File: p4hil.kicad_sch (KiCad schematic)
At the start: 9 parts, among them J10 Conn_01x22, J11 Conn_01x22, J12 Conn_01x22, J2 Conn_01x08, J4 Conn_01x10, J5 Conn_01x22, J6 Conn_01x22, J7 Conn_01x22, J9 Conn_01x06

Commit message: More brainstorming
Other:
- sheet P4 ports: added CHIP_PU, GPIO0/ADC, GPIO10/ADC, GPIO11/ADC, GPIO12/ADC, GPIO13/ADC, GPIO14/ADC, GPIO15/ADC, GPIO16/ADC, GPIO17/ADC, GPIO18/ADC, GPIO19/ADC, GPIO1/ADC, GPIO20/ADC, GPIO21/ADC, GPIO22/ADC, GPIO23/ADC, GPIO24/ADC/USB_JTAG_DM, GPIO25/ADC/USB_JTAG_DP, GPIO26/ADC/USB, GPIO27/ADC/USB, GPIO28, GPIO29, GPIO2/ADC, GPIO30, GPIO31, GPIO32, GPIO33, GPIO34, GPIO35_BOOT_PULLUP, GPIO36_PULLUP, GPIO37/UART0_TXD, GPIO38/UART0_RXD, GPIO39, GPIO3/ADC, GPIO40, GPIO41, GPIO42, GPIO43, GPIO44, GPIO45, GPIO46, GPIO47, GPIO48, GPIO49/ADC, GPIO4/ADC, GPIO50/ADC, GPIO51/ADC, GPIO52/ADC, GPIO53/ADC, GPIO54/ADC, GPIO5/ADC, GPIO6/ADC, GPIO7/ADC, GPIO8/ADC, GPIO9/ADC, HS_USB_D+, HS_USB_D-; removed none

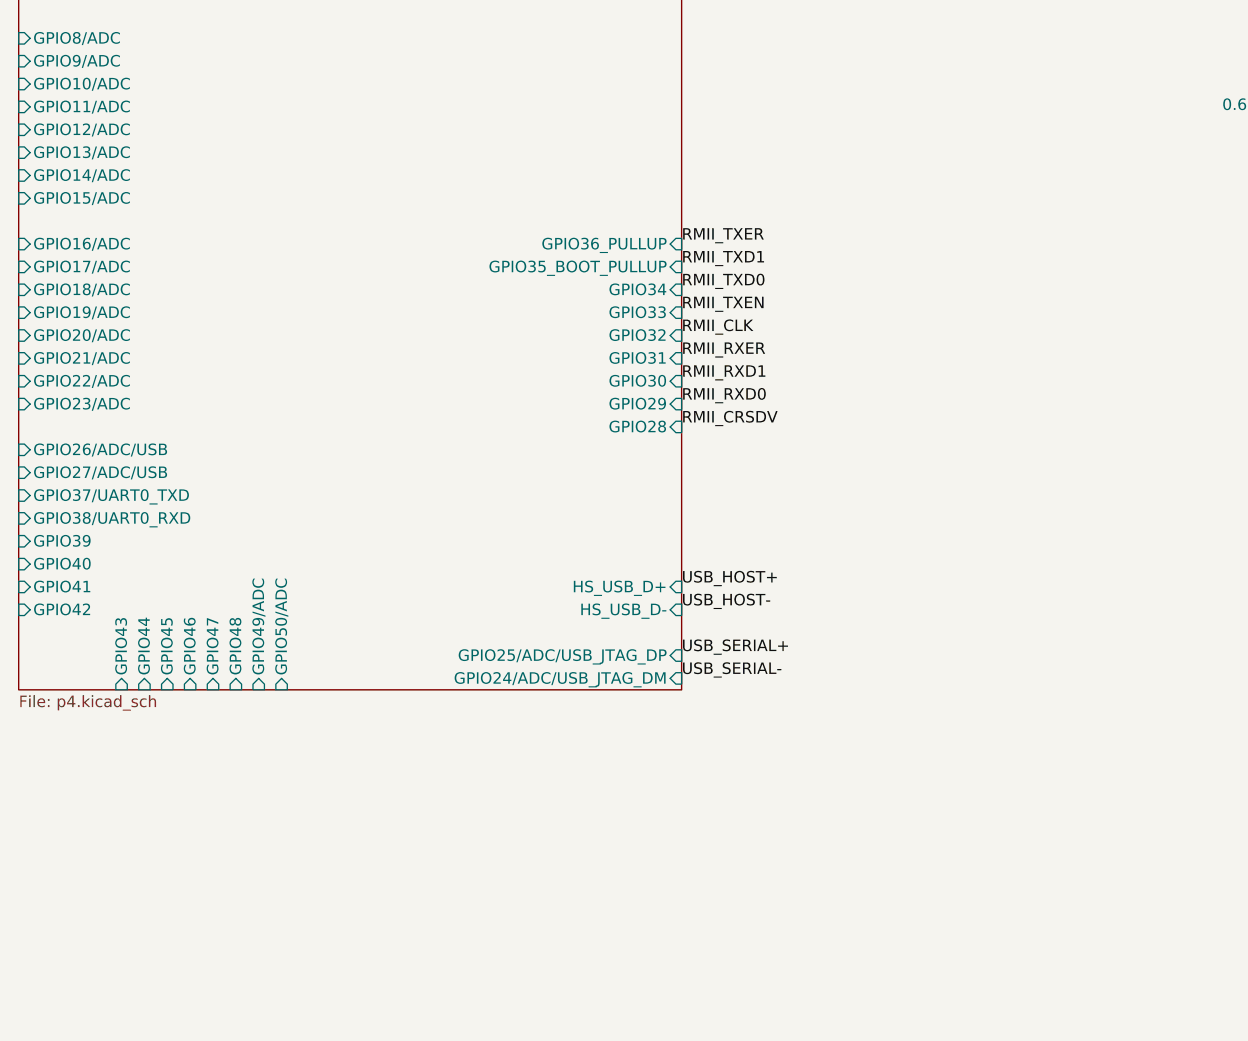
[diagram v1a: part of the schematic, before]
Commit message: More schematic work. Mostly on Ethernet
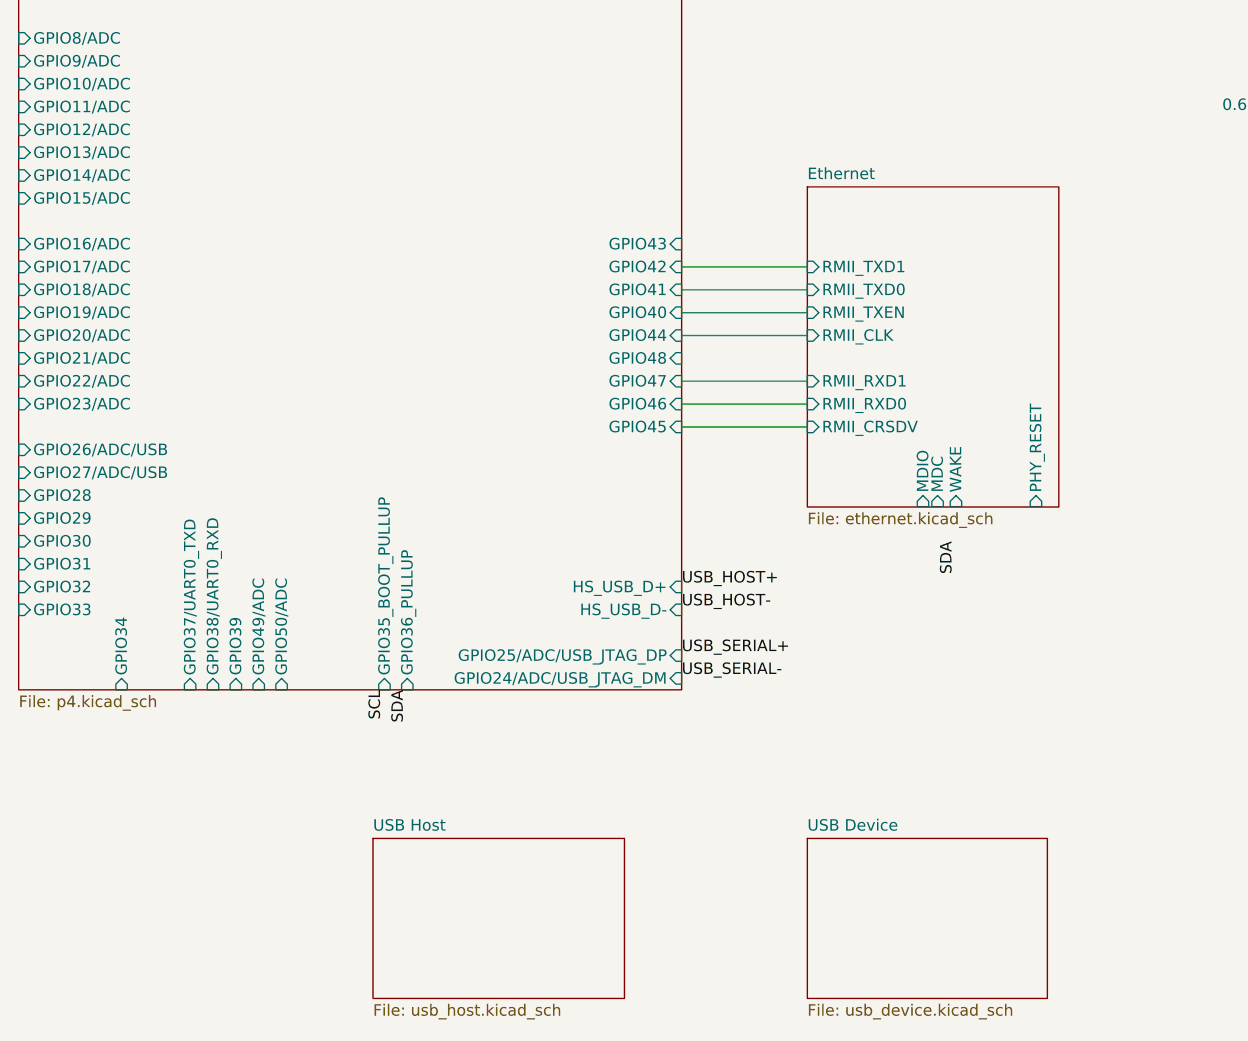
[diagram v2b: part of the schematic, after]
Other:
- added sheet Ethernet (ethernet.kicad_sch)
- added sheet USB Device (usb_device.kicad_sch)
- added sheet USB Host (usb_host.kicad_sch)

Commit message: More USB schematic work
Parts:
- added C54: 0.1uF, Capacitor_SMD:C_0402_1005Metric, symbol Device:C_Small
- added C55, C57: 10uF, Capacitor_SMD:C_0603_1608Metric, symbol Device:C_Small
- added C56: 22pF, Capacitor_SMD:C_0402_1005Metric, symbol Device:C_Small
- added D1: WS2812B, LED_SMD:LED_WS2812B_PLCC4_5.0x5.0mm_P3.2mm, symbol LED:WS2812B
- added D8: GREEN LED, Diode_SMD:D_0805_2012Metric, symbol Device:LED_Small_Filled
- added J14: Conn_01x04, Connector_JST:JST_SH_SM04B-SRSS-TB_1x04-1MP_P1.00mm_Horizontal, symbol Connector_Generic:Conn_01x04
- added J15: Conn_01x20, Connector_PinHeader_2.54mm:PinHeader_1x22_P2.54mm_Vertical, symbol Connector_Generic:Conn_01x20
- added L2: 2.2uH, Inductor_SMD:L_1008_2520Metric, symbol Device:L_Small
- added R24, R25: 4.7K, symbol Device:R_Small
- added R26: 2.2K, Resistor_SMD:R_0402_1005Metric, symbol Device:R_Small
- added R27: 10K, Resistor_SMD:R_0402_1005Metric, symbol Device:R_Small
- added R28: 100K(1%), Resistor_SMD:R_0402_1005Metric, symbol Device:R_Small
- added R29: 22.1K(1%), Resistor_SMD:R_0402_1005Metric, symbol Device:R_Small
- added SW1, SW2: SW_Push, symbol Switch:SW_Push
- added U10: TLV62569DBV, Package_TO_SOT_SMD:SOT-23-5, symbol Regulator_Switching:TLV62569DBV
- J10, J11, J12, J5, J6, J7: value Conn_01x22 -> Conn_01x20; symbol Connector_Generic:Conn_01x22 -> Connector_Generic:Conn_01x20
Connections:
- net SCL: now also J14.4 (Pin_4), R25.1
- net at J9.1 (Pin_1): now also J5.14 (Pin_14); no longer J5.7 (Pin_7)
- net at J9.2 (Pin_2): now also J5.5 (Pin_5); no longer J5.6 (Pin_6)
- net at J9.3 (Pin_3): now also J5.4 (Pin_4); no longer J5.5 (Pin_5)
- net at J9.4 (Pin_4): now also J5.3 (Pin_3); no longer J5.4 (Pin_4)
- net at J9.5 (Pin_5): now also J5.2 (Pin_2); no longer J5.3 (Pin_3)
- net at J9.6 (Pin_6): now also J5.1 (Pin_1); no longer J5.2 (Pin_2)
- net at J10.1 (Pin_1), J11.1 (Pin_1), J12.1 (Pin_1)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: now also J15.1 (Pin_1)
- net at J10.10 (Pin_10), J11.10 (Pin_10), J12.10 (Pin_10)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: now also J15.10 (Pin_10)
- net at J10.11 (Pin_11), J11.11 (Pin_11), J12.11 (Pin_11)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: now also J15.11 (Pin_11)
- net at J10.12 (Pin_12), J11.12 (Pin_12), J12.12 (Pin_12)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: now also J15.12 (Pin_12)
- net at J10.13 (Pin_13), J11.13 (Pin_13), J12.13 (Pin_13)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: now also J2.1 (Pin_1), J15.13 (Pin_13)
- net at J10.14 (Pin_14), J11.14 (Pin_14), J12.14 (Pin_14)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: now also J2.2 (Pin_2), J15.14 (Pin_14)
- net at J10.15 (Pin_15), J11.15 (Pin_15), J12.15 (Pin_15)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: now also J2.3 (Pin_3), J15.15 (Pin_15); no longer J2.1 (Pin_1)
- net at J10.16 (Pin_16), J11.16 (Pin_16), J12.16 (Pin_16)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: now also J2.4 (Pin_4), J15.16 (Pin_16); no longer J2.2 (Pin_2)
- net at J10.17 (Pin_17), J11.17 (Pin_17), J12.17 (Pin_17)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: now also J2.5 (Pin_5), J15.17 (Pin_17); no longer J2.3 (Pin_3)
- net at J10.18 (Pin_18), J11.18 (Pin_18), J12.18 (Pin_18)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: now also J2.6 (Pin_6), J15.18 (Pin_18); no longer J2.4 (Pin_4)
- net at J10.19 (Pin_19), J11.19 (Pin_19), J12.19 (Pin_19)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: now also J2.7 (Pin_7), J15.19 (Pin_19); no longer J2.5 (Pin_5)
- net at J10.2 (Pin_2), J11.2 (Pin_2), J12.2 (Pin_2)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: now also J15.2 (Pin_2)
- net at J10.20 (Pin_20), J11.20 (Pin_20), J12.20 (Pin_20)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: now also J2.8 (Pin_8), J15.20 (Pin_20); no longer J2.6 (Pin_6)
- net at J10.3 (Pin_3), J11.3 (Pin_3), J12.3 (Pin_3)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: now also J15.3 (Pin_3)
- net at J10.4 (Pin_4), J11.4 (Pin_4), J12.4 (Pin_4)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: now also J15.4 (Pin_4)
- net at J10.5 (Pin_5), J11.5 (Pin_5), J12.5 (Pin_5)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: now also J15.5 (Pin_5)
- net at J10.6 (Pin_6), J11.6 (Pin_6), J12.6 (Pin_6)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: now also J15.6 (Pin_6)
- net at J10.7 (Pin_7), J11.7 (Pin_7), J12.7 (Pin_7)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: now also J15.7 (Pin_7)
- net at J10.8 (Pin_8), J11.8 (Pin_8), J12.8 (Pin_8)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: now also J15.8 (Pin_8)
- net at J10.9 (Pin_9), J11.9 (Pin_9), J12.9 (Pin_9)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: now also J15.9 (Pin_9)
- new net: C56.2, R28.2, R29.1, U10.5 (FB)
- new net: D8.2 (A), R26.2
- new net: R27.1, U10.1 (EN)
- new net: L2.1, U10.3 (SW)
- new net +3.3V: C54.1, C56.1, C57.1, D1.1 (VDD), J14.2 (Pin_2), L2.2, R24.1, R25.2, R28.1
- new net +5V: C55.1, R26.1, R27.2, U10.4 (VIN)
- new net GND: C54.2, C55.2, C57.2, D1.3 (VSS), D8.1 (K), J14.1 (Pin_1), R29.2, SW1.1, SW2.1, U10.2 (GND)
- new net NEOPIXEL_WAKE: D1.4 (DIN)
- new net RESET: SW2.2
- new net SDA_BOOT: J14.3 (Pin_3), R24.2, SW1.2
- no-connect marks 0 -> 1
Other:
- sheet USB Device ports: added USB+, USB-; removed none
- sheet USB Host ports: added POWER_ON, SCL, SDA, USB+, USB-; removed none
- note added: "0.5" - Trinket"
- moved on the sheet: J4

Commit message: Getting close. Fault circuit left
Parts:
- removed C55, C57: 10uF, Capacitor_SMD:C_0603_1608Metric, symbol Device:C_Small
- removed C56: 22pF, Capacitor_SMD:C_0402_1005Metric, symbol Device:C_Small
- removed D8: GREEN LED, Diode_SMD:D_0805_2012Metric, symbol Device:LED_Small_Filled
- removed L2: 2.2uH, Inductor_SMD:L_1008_2520Metric, symbol Device:L_Small
- removed R26: 2.2K, Resistor_SMD:R_0402_1005Metric, symbol Device:R_Small
- removed R27: 10K, Resistor_SMD:R_0402_1005Metric, symbol Device:R_Small
- removed R28: 100K(1%), Resistor_SMD:R_0402_1005Metric, symbol Device:R_Small
- removed R29: 22.1K(1%), Resistor_SMD:R_0402_1005Metric, symbol Device:R_Small
- removed U10: TLV62569DBV, Package_TO_SOT_SMD:SOT-23-5, symbol Regulator_Switching:TLV62569DBV
- J10, J11, J12, J15, J5, J6, J7: footprint Connector_PinHeader_2.54mm:PinHeader_1x22_P2.54mm_Vertical -> Connector_PinHeader_2.54mm:PinHeader_1x20_P2.54mm_Vertical
- R24, R25: footprint (none) -> Resistor_SMD:R_0402_1005Metric
- SW1, SW2: footprint (none) -> Button_Switch_SMD:SW_Push_1P1T-MP_NO_Horizontal_Alps_SKRTLAE010
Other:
- added sheet Power Options (power_options.kicad_sch)
- sheet Ethernet ports: added POWER1, POWER2; removed none
- sheet USB Device ports: added USB_5V; removed none

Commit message: Fault circuit getting close
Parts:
- removed J10, J11, J12, J15, J5, J6, J7: Conn_01x20, Connector_PinHeader_2.54mm:PinHeader_1x20_P2.54mm_Vertical, symbol Connector_Generic:Conn_01x20
- removed J2: Conn_01x08, Connector_PinHeader_2.54mm:PinHeader_1x08_P2.54mm_Vertical, symbol Connector_Generic:Conn_01x08
- removed J4: Conn_01x10, Connector_PinHeader_2.54mm:PinHeader_1x10_P2.54mm_Vertical, symbol Connector_Generic:Conn_01x10
- removed J9: Conn_01x06, Connector_PinHeader_2.54mm:PinHeader_1x06_P2.54mm_Vertical, symbol Connector_Generic:Conn_01x06
- added D26: RED, symbol Device:LED_Small
- D1: footprint LED_SMD:LED_WS2812B_PLCC4_5.0x5.0mm_P3.2mm -> WorldSemi:WS2812B-4020
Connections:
- net GND: now also D26.1 (K)
- new net FaultCheck/FAULT: D26.2 (A)
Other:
- added sheet DeviceUnderTest (dut.kicad_sch)
- added sheet FaultCheck (faultcheck.kicad_sch)
- note removed: "-0.1" - Arduino analog header"
- note removed: "0" - Inset arduino header"
- note removed: "0.5" - Trinket"
- note removed: "0.6" - XIAO, QTPy, Teensy, Nano"
- note removed: "0.7" - Pico"
- note removed: "0.8" - Feather"
- note removed: "0.9" - ESP32S3"
- note removed: "1" - ESP32"
- note removed: "Skip the power Arduino header in favor of inset extras."
- moved on the sheet: J14, R24, R25, SW1, SW2

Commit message: where I'm at. fault not needed
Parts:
- D26: footprint (none) -> LED_SMD:LED_0603_1608Metric
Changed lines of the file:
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@@
 			)
 		)
-		(property "Footprint" ""
+		(property "Footprint" "LED_SMD:LED_0603_1608Metric"
 			(at 74.93 177.8 90)
 			(hide yes)

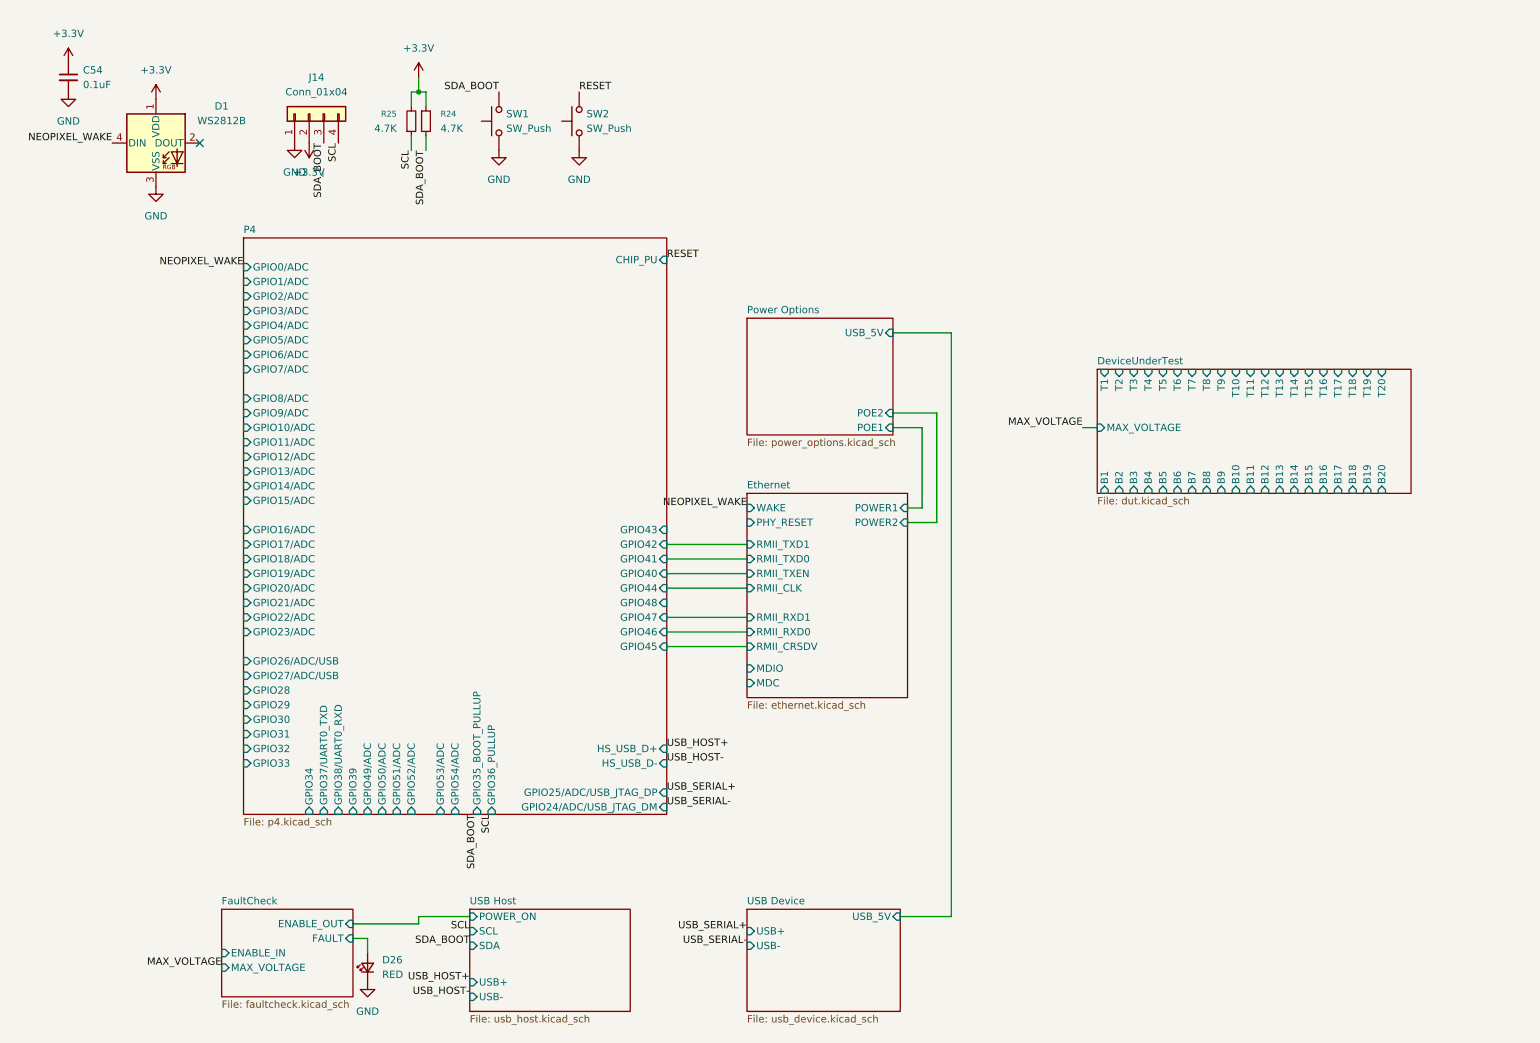
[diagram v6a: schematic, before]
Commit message: Remove fault stuff
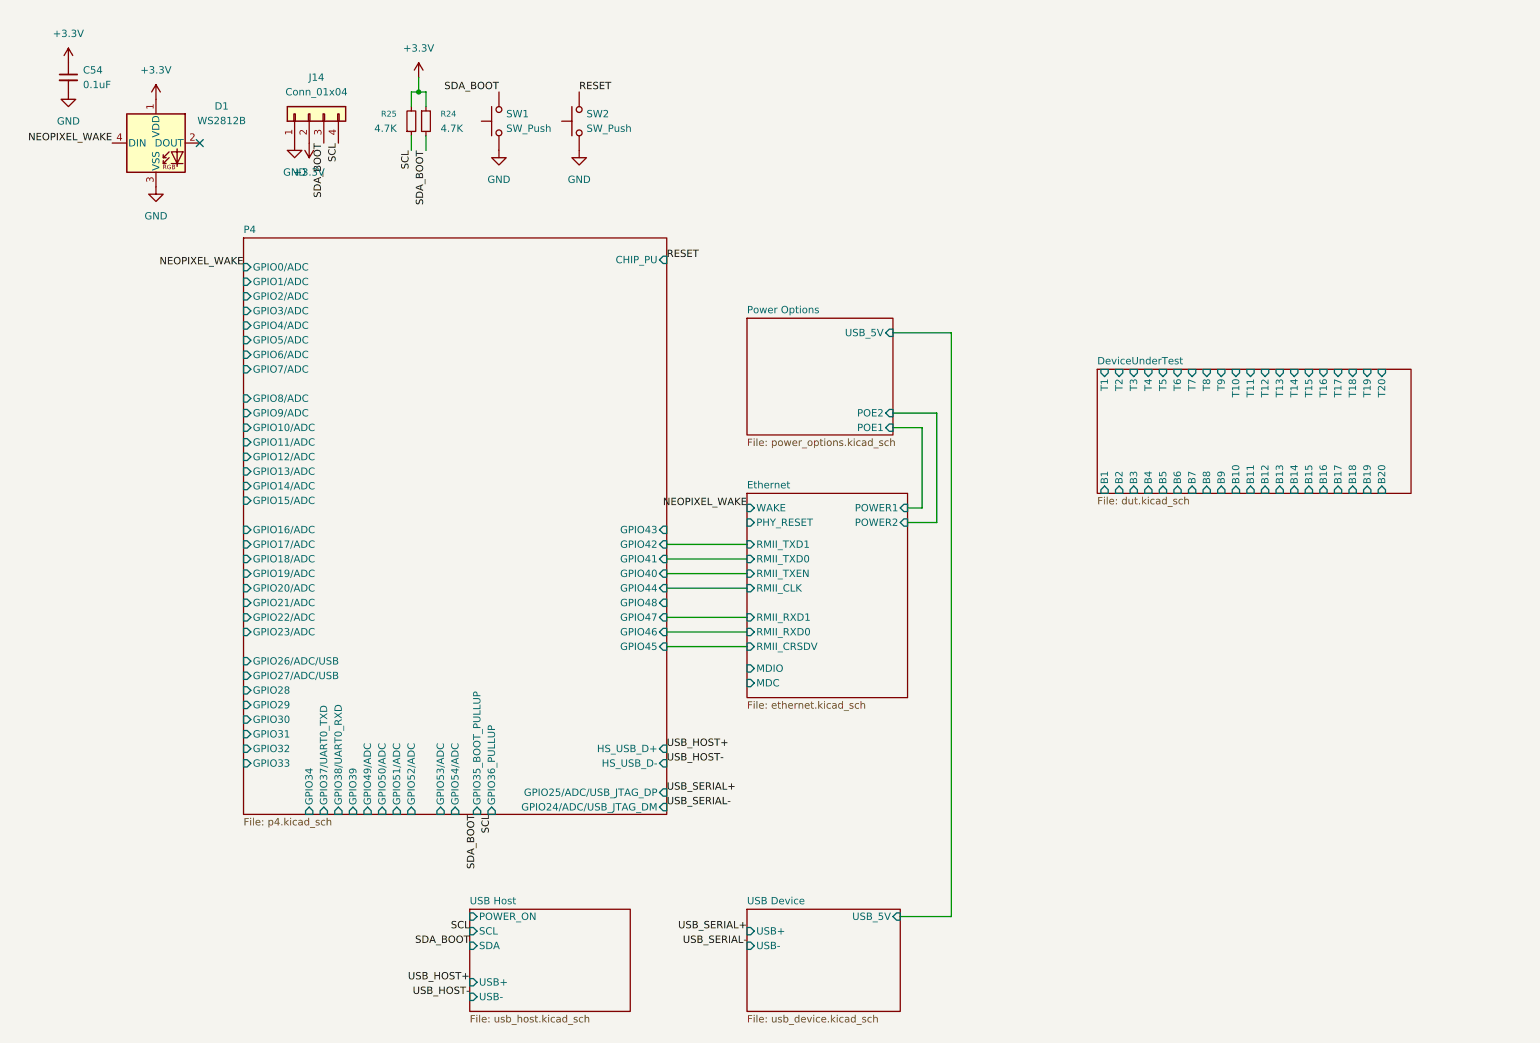
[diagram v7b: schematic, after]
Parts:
- removed D26: RED, LED_SMD:LED_0603_1608Metric, symbol Device:LED_Small
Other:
- removed sheet FaultCheck
- sheet DeviceUnderTest ports: added none; removed MAX_VOLTAGE

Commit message: Drop T20'
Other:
- sheet DeviceUnderTest ports: added none; removed T20
